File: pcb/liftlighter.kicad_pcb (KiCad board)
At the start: 2 copper layers, 60 x 90 mm, 54 parts, among them IC1 ATMEGA8-P, P1 CONN_01X06, P12 CONN_01X02, P2 CONN_02X10, P3 CONN_01X02, Q1 BC548, Q10 BC548, Q2 BC548, Q3 BC548, Q4 BC548, Q5 BC548, Q6 BC548, Q7 BC548, Q8 BC548, Q9 BC548, SW1 SW_PUSH, SW2 SW_PUSH, U1 LD1117S33TR, Y1 Crystal

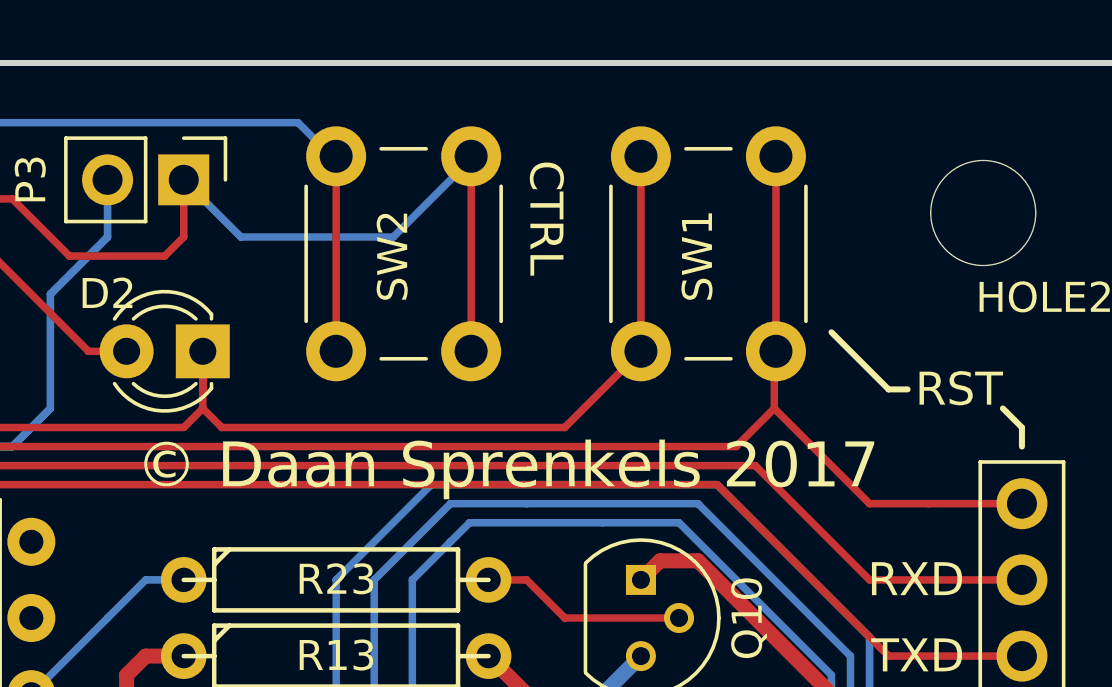
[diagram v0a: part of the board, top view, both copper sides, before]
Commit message: Add time control functionality
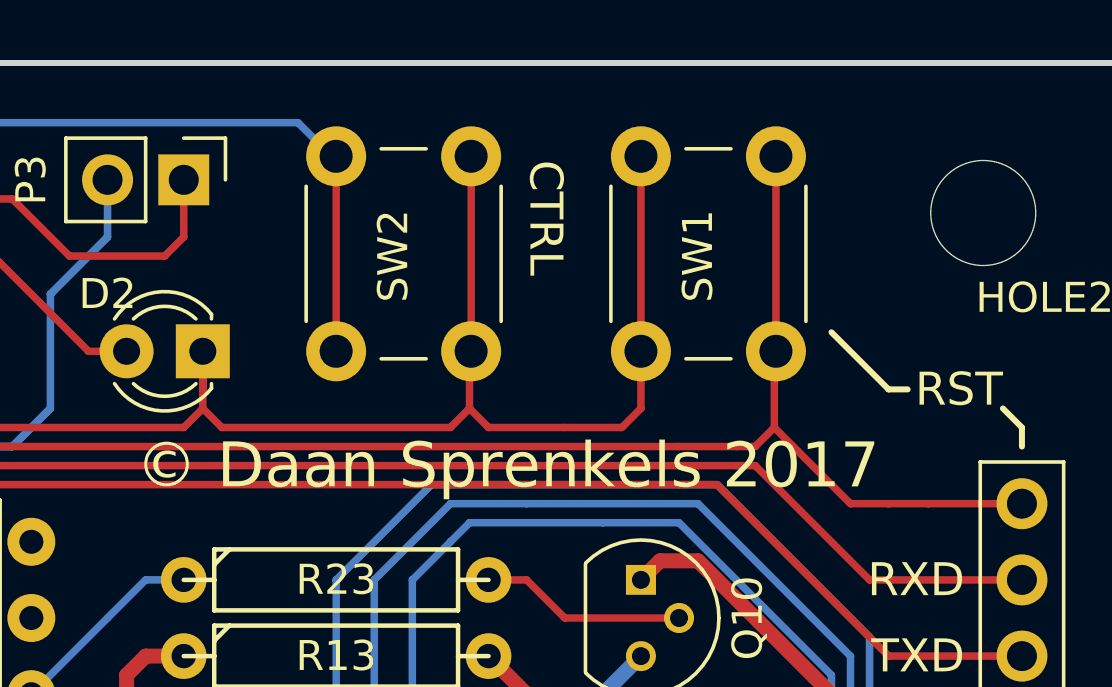
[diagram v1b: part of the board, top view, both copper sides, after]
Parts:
- R2: value 10K -> 50K
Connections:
- SW2 pad 2: VCC -> GND
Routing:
- net VCC: track 140.3 -> 122.2 mm
- net GND: track 230.7 -> 240.9 mm
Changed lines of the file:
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@@
     (thickness 1.6)
     (drawings 23)
-    (tracks 538)
+    (tracks 545)
     (zones 0)
     (modules 54)
@@
     (fp_circle (center 3.25 2.25) (end 1.25 2.5) (layer F.Fab) (width 0.1))
     (pad 2 thru_hole circle (at 0 4.5 180) (size 2 2) (drill 1.1) (layers *.Cu *.Mask)
-      (net 4 VCC))
+      (net 2 GND))
     (pad 1 thru_hole circle (at 0 0 180) (size 2 2) (drill 1.1) (layers *.Cu *.Mask)
       (net 31 "Net-(IC1-Pad4)"))
     (pad 2 thru_hole circle (at 6.5 4.5 180) (size 2 2) (drill 1.1) (layers *.Cu *.Mask)
-      (net 4 VCC))
+      (net 2 GND))
     (pad 1 thru_hole circle (at 6.5 0 180) (size 2 2) (drill 1.1) (layers *.Cu *.Mask)
       (net 31 "Net-(IC1-Pad4)"))
@@
       (effects (font (size 1 1) (thickness 0.15)))
     )
-    (fp_text value 10K (at 0 0 180) (layer F.Fab)
+    (fp_text value 50K (at 0 0 180) (layer F.Fab)
       (effects (font (size 1 1) (thickness 0.15)))
     )
@@
   (segment (start 112.395 118.745) (end 112.395 111.125) (width 0.25) (layer F.Cu) (net 1))
   (segment (start 117.475 123.825) (end 112.395 118.745) (width 0.25) (layer F.Cu) (net 1))
+  (segment (start 146.05 57.15) (end 147.955 57.15) (width 0.25) (layer F.Cu) (net 2))
+  (segment (start 148.59 56.515) (end 148.59 54.61) (width 0.25) (layer F.Cu) (net 2) (status 800000))
+  (segment (start 147.955 57.15) (end 148.59 56.515) (width 0.25) (layer F.Cu) (net 2))
+  (segment (start 142.93 54.61) (end 142.875 54.61) (width 0.25) (layer B.Cu) (net 2))
+  (segment (start 142.24 57.15) (end 142.875 56.515) (width 0.25) (layer F.Cu) (net 2))
+  (segment (start 142.875 56.515) (end 142.875 54.665) (width 0.25) (layer F.Cu) (net 2))
+  (segment (start 143.51 57.15) (end 146.05 57.15) (width 0.25) (layer F.Cu) (net 2))
+  (segment (start 142.875 56.515) (end 143.51 57.15) (width 0.25) (layer F.Cu) (net 2))
+  (segment (start 142.875 54.665) (end 142.93 54.61) (width 0.25) (layer F.Cu) (net 2))
   (segment (start 110.49 92.71) (end 110.49 91.44) (width 0.25) (layer F.Cu) (net 2))
   (segment (start 116.84 90.17) (end 118.11 91.44) (width 0.25) (layer F.Cu) (net 2))
@@
   (segment (start 133.985 55.88) (end 133.985 54.61) (width 0.25) (layer F.Cu) (net 2))
   (segment (start 133.985 56.515) (end 134.62 57.15) (width 0.25) (layer F.Cu) (net 2))
-  (segment (start 134.62 57.15) (end 146.05 57.15) (width 0.25) (layer F.Cu) (net 2))
+  (segment (start 134.62 57.15) (end 142.24 57.15) (width 0.25) (layer F.Cu) (net 2))
   (segment (start 133.985 55.245) (end 133.985 55.88) (width 0.25) (layer F.Cu) (net 2))
   (segment (start 133.985 55.88) (end 133.985 56.515) (width 0.25) (layer F.Cu) (net 2))
-  (segment (start 146.05 57.15) (end 148.59 54.61) (width 0.25) (layer F.Cu) (net 2))
   (segment (start 148.59 48.11) (end 148.59 54.61) (width 0.25) (layer F.Cu) (net 2))
+  (segment (start 142.93 48.11) (end 142.93 48.205) (width 0.25) (layer B.Cu) (net 2))
+  (segment (start 142.93 48.11) (end 142.93 54.61) (width 0.25) (layer F.Cu) (net 2))
   (segment (start 133.35 128.27) (end 133.35 121.92) (width 0.5) (layer F.Cu) (net 3))
   (segment (start 114.3 100.33) (end 114.3 104.14) (width 0.5) (layer B.Cu) (net 3))
@@
   (segment (start 123.825 53.34) (end 125.095 54.61) (width 0.25) (layer F.Cu) (net 4))
   (segment (start 125.095 54.61) (end 126.365 54.61) (width 0.25) (layer F.Cu) (net 4))
-  (segment (start 142.93 48.11) (end 142.93 48.205) (width 0.25) (layer B.Cu) (net 4))
-  (segment (start 142.93 48.205) (end 140.335 50.8) (width 0.25) (layer B.Cu) (net 4))
-  (segment (start 135.255 50.8) (end 133.35 48.895) (width 0.25) (layer B.Cu) (net 4))
-  (segment (start 140.335 50.8) (end 135.255 50.8) (width 0.25) (layer B.Cu) (net 4))
   (segment (start 113.03 92.71) (end 113.03 93.98) (width 0.25) (layer B.Cu) (net 4))
   (segment (start 113.03 93.98) (end 116.84 97.79) (width 0.25) (layer B.Cu) (net 4))
   (segment (start 124.46 97.79) (end 125.73 99.06) (width 0.25) (layer B.Cu) (net 4))
   (segment (start 116.84 97.79) (end 124.46 97.79) (width 0.25) (layer B.Cu) (net 4))
-  (segment (start 142.93 54.61) (end 142.875 54.61) (width 0.25) (layer B.Cu) (net 4))
   (segment (start 120.65 76.2) (end 119.38 76.2) (width 0.25) (layer B.Cu) (net 4))
   (segment (start 113.03 87.63) (end 113.03 93.98) (width 0.25) (layer B.Cu) (net 4))
@@
   (segment (start 117.475 78.105) (end 117.475 83.185) (width 0.25) (layer B.Cu) (net 4))
   (segment (start 119.38 76.2) (end 117.475 78.105) (width 0.25) (layer B.Cu) (net 4))
-  (segment (start 142.93 48.11) (end 142.93 54.61) (width 0.25) (layer F.Cu) (net 4))
   (segment (start 120.65 76.2) (end 121.92 76.2) (width 0.25) (layer F.Cu) (net 4))
   (segment (start 121.92 76.2) (end 127 81.28) (width 0.25) (layer F.Cu) (net 4))
@@
   (segment (start 130.175 54.61) (end 127 51.435) (width 0.25) (layer F.Cu) (net 5))
   (segment (start 127 51.435) (end 126.365 51.435) (width 0.25) (layer F.Cu) (net 5))
+  (segment (start 153.035 57.15) (end 153.035 54.665) (width 0.25) (layer F.Cu) (net 6) (status 800000))
+  (segment (start 153.035 54.665) (end 153.09 54.61) (width 0.25) (layer F.Cu) (net 6) (status C00000))
+  (segment (start 151.765 57.785) (end 152.4 57.785) (width 0.25) (layer F.Cu) (net 6))
+  (segment (start 155.575 59.69) (end 156.845 59.69) (width 0.25) (layer F.Cu) (net 6))
+  (segment (start 153.035 57.15) (end 155.575 59.69) (width 0.25) (layer F.Cu) (net 6))
+  (segment (start 152.4 57.785) (end 153.035 57.15) (width 0.25) (layer F.Cu) (net 6))
   (segment (start 120.65 57.785) (end 120.65 56.515) (width 0.25) (layer B.Cu) (net 6))
   (segment (start 118.745 54.61) (end 116.205 54.61) (width 0.25) (layer B.Cu) (net 6))
   (segment (start 120.65 56.515) (end 118.745 54.61) (width 0.25) (layer B.Cu) (net 6))
   (segment (start 120.65 57.785) (end 120.65 60.96) (width 0.25) (layer B.Cu) (net 6))
-  (segment (start 153.035 56.515) (end 153.035 54.665) (width 0.25) (layer F.Cu) (net 6))
   (segment (start 153.035 54.665) (end 153.09 54.61) (width 0.25) (layer F.Cu) (net 6))
   (segment (start 149.86 57.785) (end 151.765 57.785) (width 0.25) (layer F.Cu) (net 6))
-  (segment (start 156.21 59.69) (end 158.17 59.69) (width 0.25) (layer F.Cu) (net 6))
-  (segment (start 153.035 56.515) (end 156.21 59.69) (width 0.25) (layer F.Cu) (net 6))
-  (segment (start 151.765 57.785) (end 153.035 56.515) (width 0.25) (layer F.Cu) (net 6))
+  (segment (start 156.845 59.69) (end 158.17 59.69) (width 0.25) (layer F.Cu) (net 6))
   (segment (start 161.29 59.69) (end 158.17 59.69) (width 0.25) (layer F.Cu) (net 6))
   (segment (start 120.65 60.96) (end 123.825 57.785) (width 0.25) (layer F.Cu) (net 6))

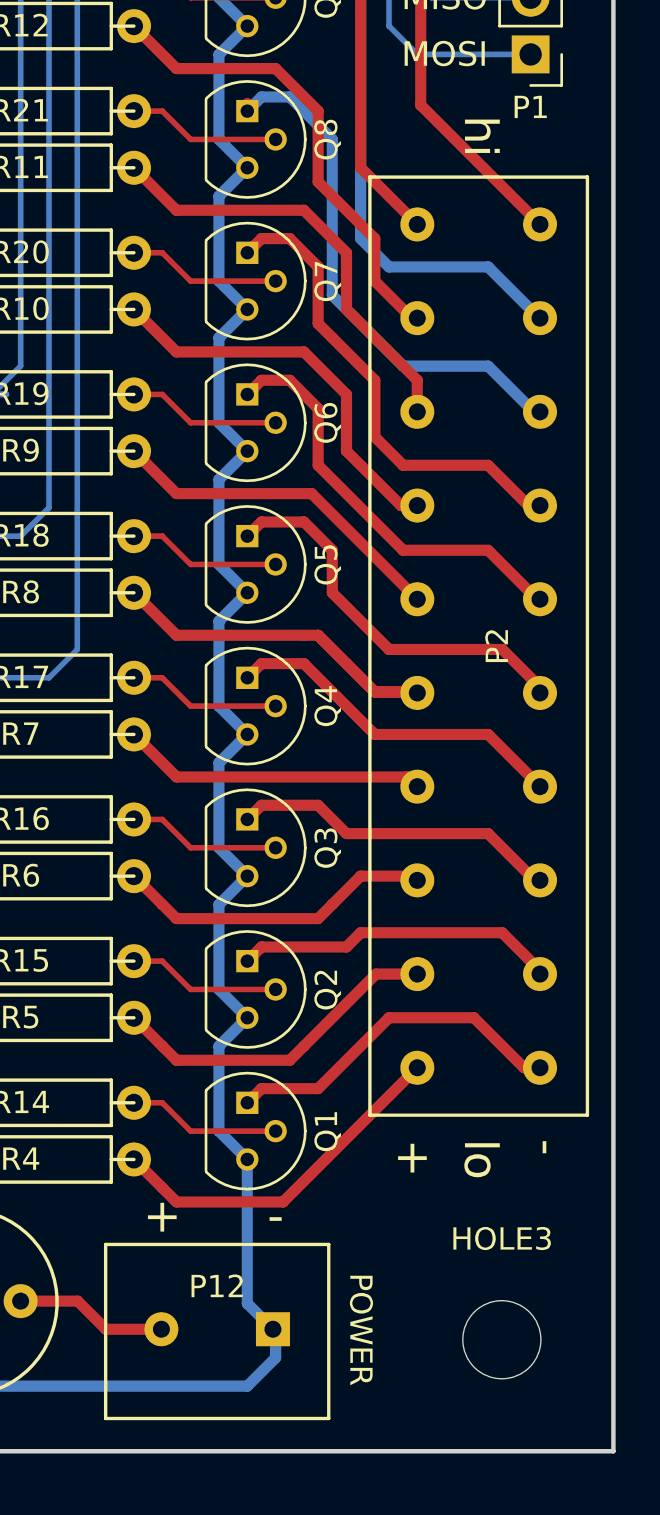
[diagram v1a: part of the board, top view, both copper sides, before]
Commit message: Increase drill hole size for TE connector
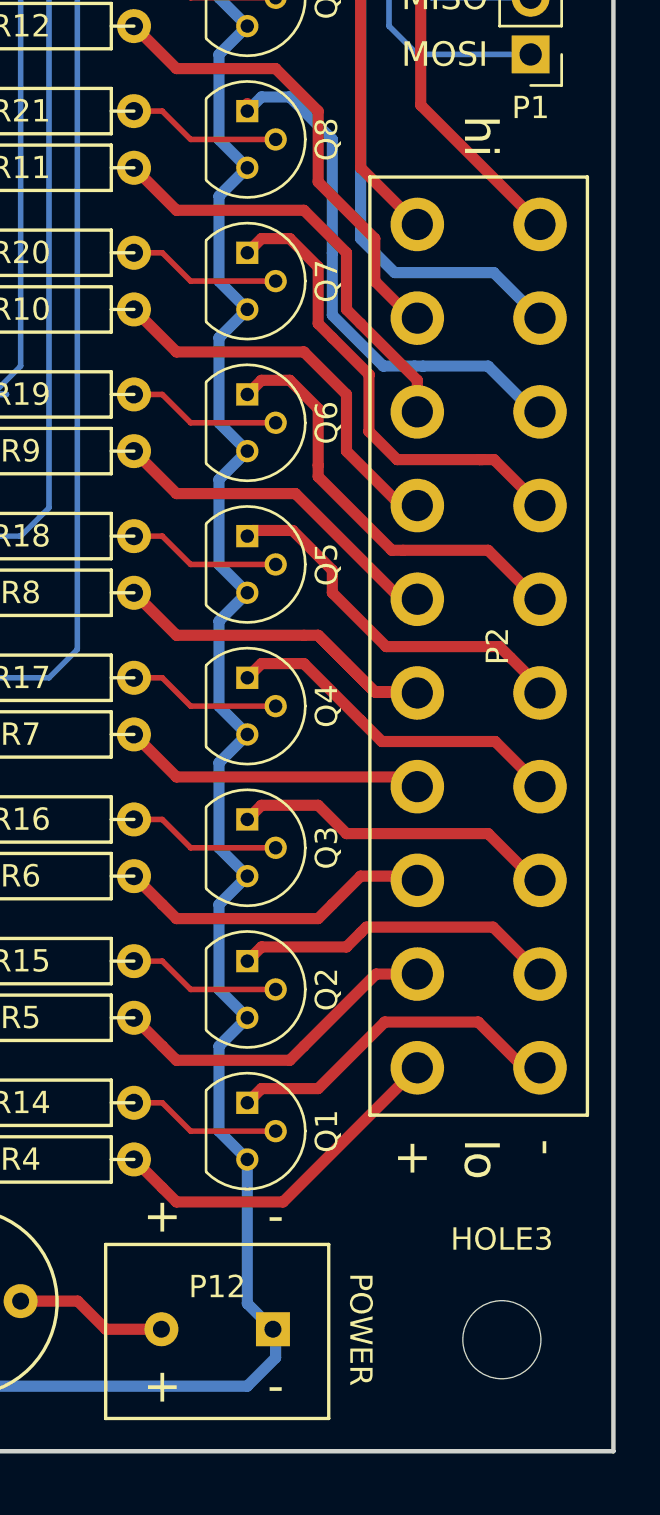
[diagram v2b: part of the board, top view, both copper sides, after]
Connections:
- IC1 pad 12: (no net) -> Net-(IC1-Pad12)
- IC1 pad 13: (no net) -> Net-(IC1-Pad13)
- IC1 pad 21: (no net) -> Net-(IC1-Pad21)
- IC1 pad 27: (no net) -> Net-(IC1-Pad27)
- IC1 pad 28: (no net) -> Net-(IC1-Pad28)
- IC1 pad 5: (no net) -> Net-(IC1-Pad5)
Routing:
- net Net-(P2-Pad12): track 17.8 -> 17.0 mm
- net Net-(P2-Pad8): track 21.3 -> 22.0 mm
- net Net-(P2-Pad6): track 23.7 -> 24.2 mm
